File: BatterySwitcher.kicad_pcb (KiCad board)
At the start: 2 copper layers, 17.5 x 6.5 mm, 5 parts, among them J1 Battery, J2 Power +, J3 Power -

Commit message: fixed header pins polarity
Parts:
- moved J2 15.5 mm to (156.5, 62.5)
- moved J3 15.5 mm to (141.0, 62.5)
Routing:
- net Battery  -: track 14.0 -> 4.27 mm
- net Power  + : track 10.3 -> 6.83 mm
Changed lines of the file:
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@@
 	(footprint "Connector_PinHeader_1.00mm:PinHeader_1x01_P1.00mm_Vertical"
 		(layer "B.Cu")
-		(at 141 62.5 180)
+		(at 156.5 62.5 180)
 		(descr "Through hole straight pin header, 1x01, 1.00mm pitch, single row")
 		(tags "Through hole pin header THT 1x01 1.00mm single row")
 		(property "Reference" "J2"
-			(at -2 0 180)
+			(at 1.5 0.5 180)
 			(layer "B.SilkS")
 			(effects
@@
 	(footprint "Connector_PinHeader_1.00mm:PinHeader_1x01_P1.00mm_Vertical"
 		(layer "B.Cu")
-		(at 156.5 62.5 180)
+		(at 141 62.5 180)
 		(descr "Through hole straight pin header, 1x01, 1.00mm pitch, single row")
 		(tags "Through hole pin header THT 1x01 1.00mm single row")
 		(property "Reference" "J3"
-			(at 2 0 180)
+			(at -2 0.5 180)
 			(layer "B.SilkS")
 			(effects
@@
 	)
 	(segment
-		(start 149 62)
+		(start 156 62)
+		(end 152 62)
+		(width 0.2)
+		(layer "F.Cu")
+		(net 2)
+	)
+	(segment
+		(start 152 62)
 		(end 150.5 63.5)
 		(width 0.2)
-		(layer "B.Cu")
+		(layer "F.Cu")
 		(net 2)
 	)
 	(segment
-		(start 141 62.5)
-		(end 141.5 62)
+		(start 156.5 62.5)
+		(end 156 62)
 		(width 0.2)
-		(layer "B.Cu")
+		(layer "F.Cu")
 		(net 2)
 	)
 	(segment
-		(start 141.5 62)
-		(end 149 62)
-		(width 0.2)
-		(layer "B.Cu")
-		(net 2)
-	)
-	(segment
-		(start 154 65)
-		(end 156.5 62.5)
+		(start 142.25 62.5)
+		(end 143.5 63.75)
 		(width 0.2)
 		(layer "F.Cu")
@@
 	)
 	(segment
-		(start 143.5 65)
-		(end 154 65)
+		(start 141 62.5)
+		(end 142.25 62.5)
 		(width 0.2)
 		(layer "F.Cu")
+		(net 3)
+	)
+	(segment
+		(start 143.5 63.75)
+		(end 143.5 65)
+		(width 0.2)
+		(layer "F.Cu")

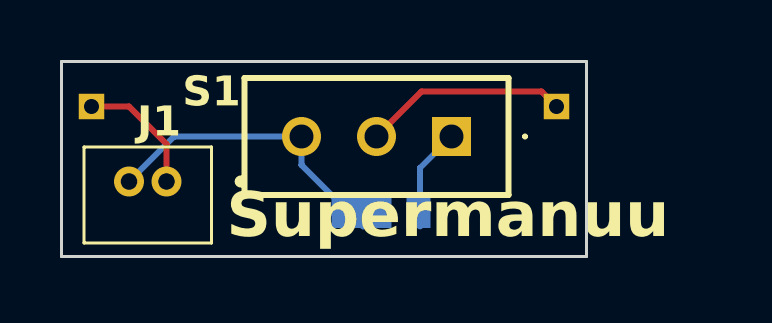
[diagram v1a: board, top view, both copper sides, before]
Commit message: changed arrange to 5mm
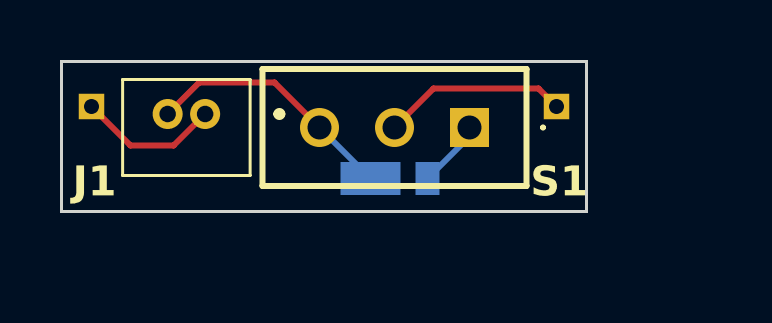
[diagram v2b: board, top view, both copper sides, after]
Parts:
- moved J1 2.59 mm to (144.8, 62.8)
- moved D1 1.14 mm to (151.2, 64.9)
- moved S1 0.67 mm to (153.6, 63.2)
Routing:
- net Battery  +: track 10.2 -> 8.52 mm
- net Net-(D1-A): track 3.43 -> 2.28 mm
- net Power  + : track 6.83 -> 6.19 mm
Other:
- board size 17.5 x 6.5 mm -> 17.5 x 5 mm
- board text removed: "Supermanuu"
